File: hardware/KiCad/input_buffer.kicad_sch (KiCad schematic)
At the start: 20 parts, among them U2 Opamp_Dual, U3 Opamp_Dual

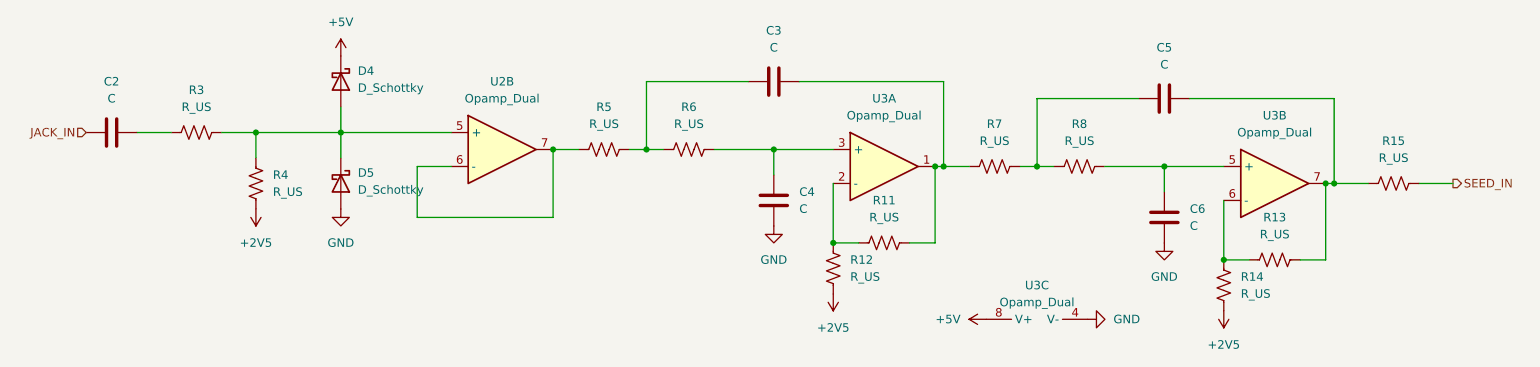
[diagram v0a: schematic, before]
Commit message: KiCad schematics on +3V3 single-supply.
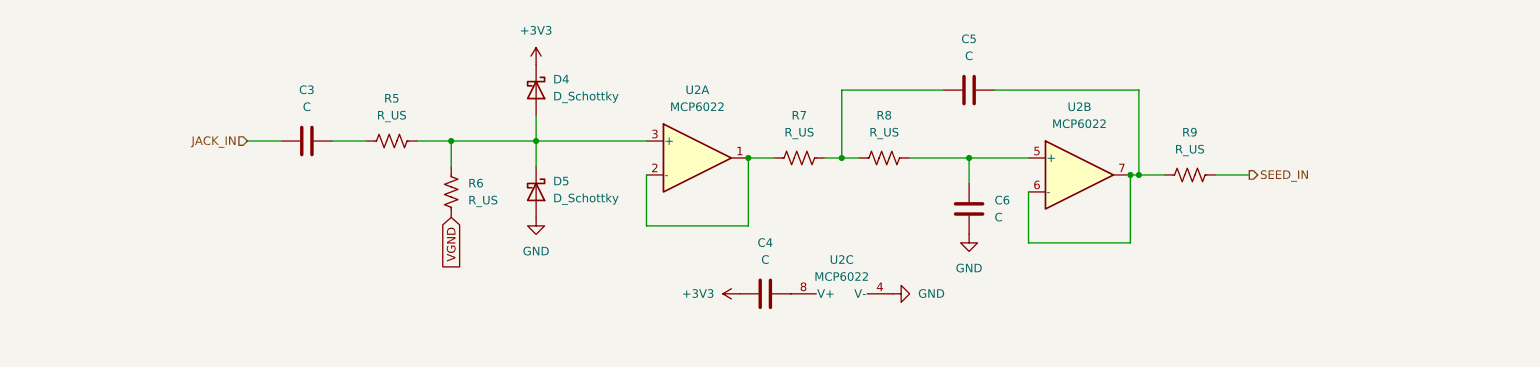
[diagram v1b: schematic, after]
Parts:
- removed C5, C6: C, symbol Device:C
- removed R11, R12, R13, R14, R15, R8: R_US, symbol Device:R_US
- removed U2, U3: Opamp_Dual, symbol Device:Opamp_Dual
- added C4: C, symbol Device:C
- added U2: MCP6022, symbol Amplifier_Operational:MCP6022
- renumbered C2 to C3, C3 to C5, C4 to C6, R3 to R5, R4 to R6, R5 to R7, R6 to R8, R7 to R9
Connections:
- net GND: now also U2.4 (V-)
- net SEED_IN: now also R9.2
- net at C5.2, R9.1: now also U2.6 (-), U2.7
- net at D4.2 (A), D5.1 (K), R5.2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: now also U2.3 (+)
- net at R7.1: now also U2.1, U2.2 (-)
- net at C6.1, R8.2: now also U2.5 (+)
- net +2V5 renamed VGND
- net +5V renamed +3V3
- net +3V3: now also C4.1
- new net: C4.2, U2.8 (V+)
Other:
- moved on the sheet: C3, C5, C6, D4, D5, R5, R6, R7, R8, R9

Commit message: Input buffer simplification; removal of BAS70-04 diodes.
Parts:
- removed D4, D5: D_Schottky, symbol Device:D_Schottky
- C3: value C -> 1µ
- C4: value C -> 0µ1
- C5: value C -> 1n
- C6: value C -> 470p
- R5: value R_US -> 1M
- R6: value R_US -> 330k
- R7, R8: value R_US -> 12k
- R9: value R_US -> 100R
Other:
- moved on the sheet: C3, C4, C5, C6, R5, R6, R7, R8, R9, U2A, U2B, U2C

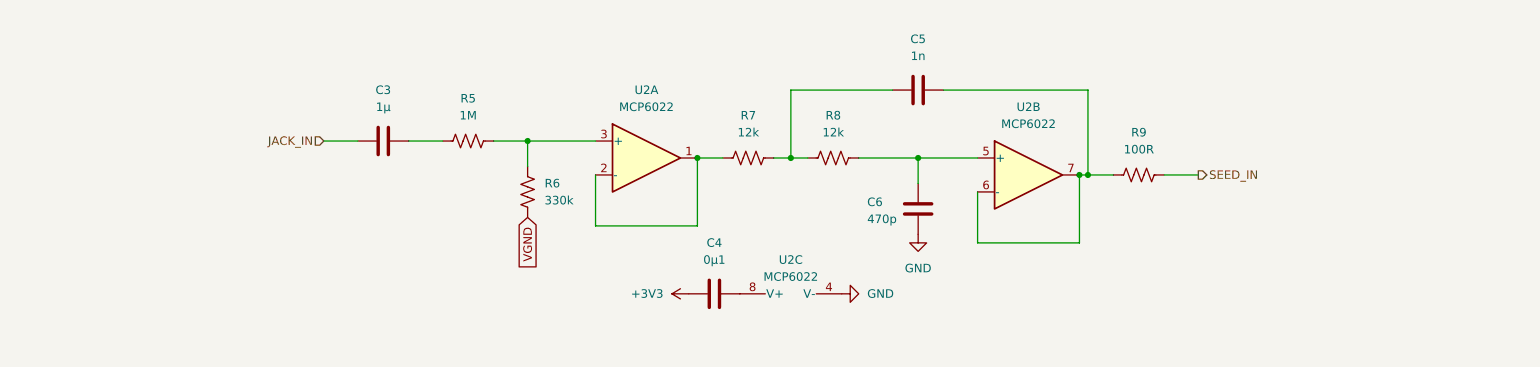
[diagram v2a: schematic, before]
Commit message: Reduction in number of op amps from 5 to 4.
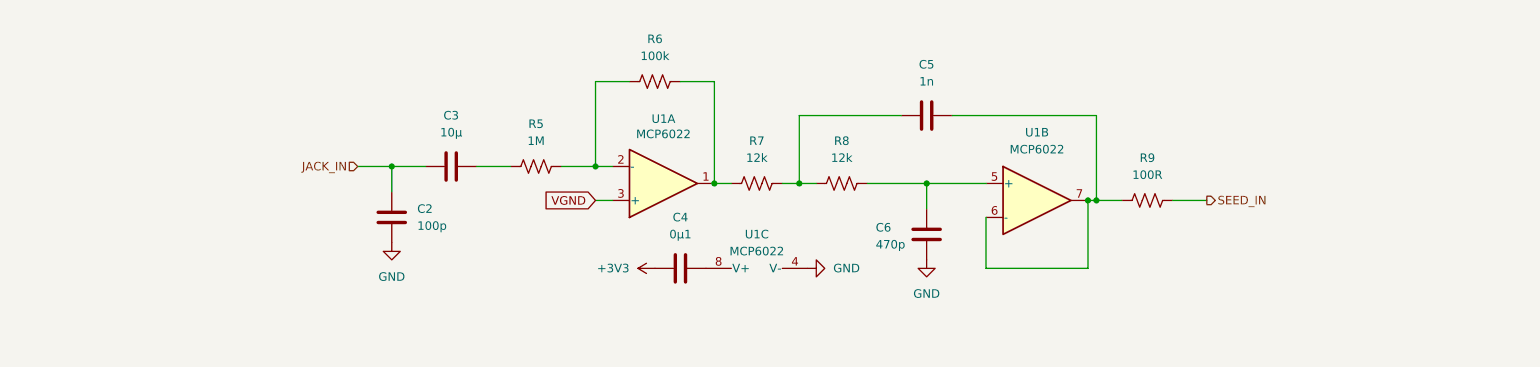
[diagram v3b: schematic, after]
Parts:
- added C2: 100p, symbol Device:C
- C3: value 1µ -> 10µ
- R6: value 330k -> 100k
- renumbered U2 to U1
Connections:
- net GND: now also C2.2
- net JACK_IN: now also C2.1
- net VGND: now also U1.3 (+); no longer R6.2
- net at R5.2, R6.1: now also U1.2 (-); no longer U1.3 (+)
- net at R7.1, U1.1: now also R6.2; no longer U1.2 (-)
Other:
- moved on the sheet: C3, C4, C5, C6, R5, R7, R8, R9, U1A, U1B, U1C
